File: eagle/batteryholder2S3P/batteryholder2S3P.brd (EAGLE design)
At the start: 144 x 90 mm, 12 parts, among them J3 POWER_JACKPTH_BREAD

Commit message: batteryholder boards minor changes
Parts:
- removed BT5, BT6, BT7: KEYSTONE_1048KEYSTONE_1048_0_0, Keystone - 1048:KEYSTONE_1048_0
- J3: value POWER_JACKPTH_BREAD -> 5.5x2.1mm Barrel; device SparkFun-Connectors:POWER_JACK_PTH_BREAD -> SparkFun-Connectors:POWER_JACK_SMD
- moved J3 6.00 mm to (141.5, 57.0), turned to 180 degrees
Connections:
- net BOTTOM_MINUS: now also BT1.2, BT1.4, BT2.2, J3.P$4; no longer BT5.1, BT5.3, BT6.1, BT6.3, BT7.1, BT7.3, J3.GND
- net TOP_MINUS: no longer BT5.2, BT5.4, BT6.2, BT6.4, BT7.2, BT7.4
- net TOP_PLUS: now also J3.VIN0; no longer BT1.2, BT1.4, BT2.2, J3.PWR
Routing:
- net TOP_PLUS: track 21.7 -> 18.2 mm
- net TOP_MINUS: vias 31 -> 0
- net BOTTOM_MINUS: vias 0 -> 66
- added copper zone on layer 1, net BOTTOM_MINUS
- removed copper zone on layer 16, net TOP_MINUS
- removed copper zone on layer 16, net TOP_PLUS
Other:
- board text added: "2S3P"
- board text added: "batteryholder 2S3P"
- board text added: "revision B"
- board text removed: "2S6P"

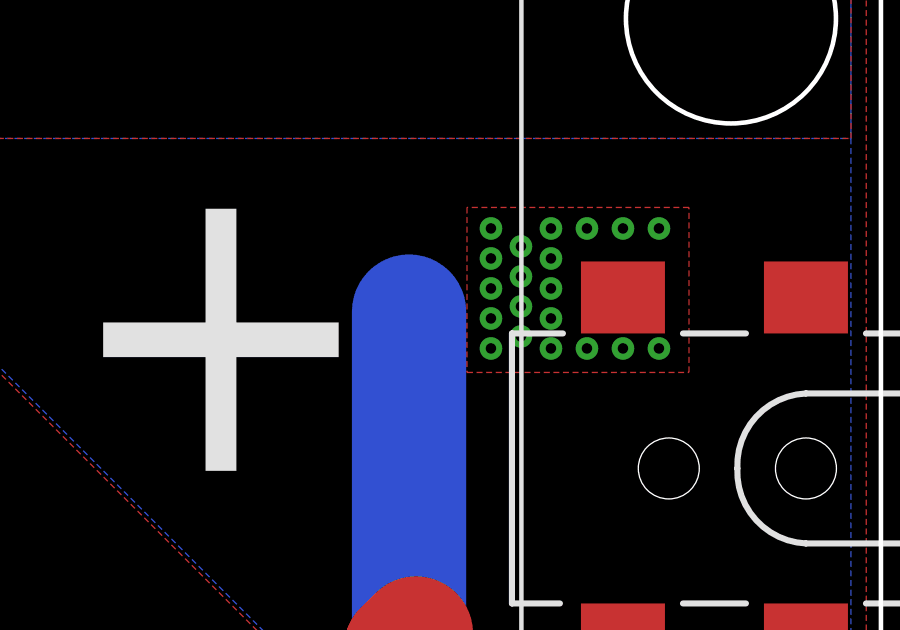
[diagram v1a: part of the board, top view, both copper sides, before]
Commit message: eagle: rename batteryholder vertical
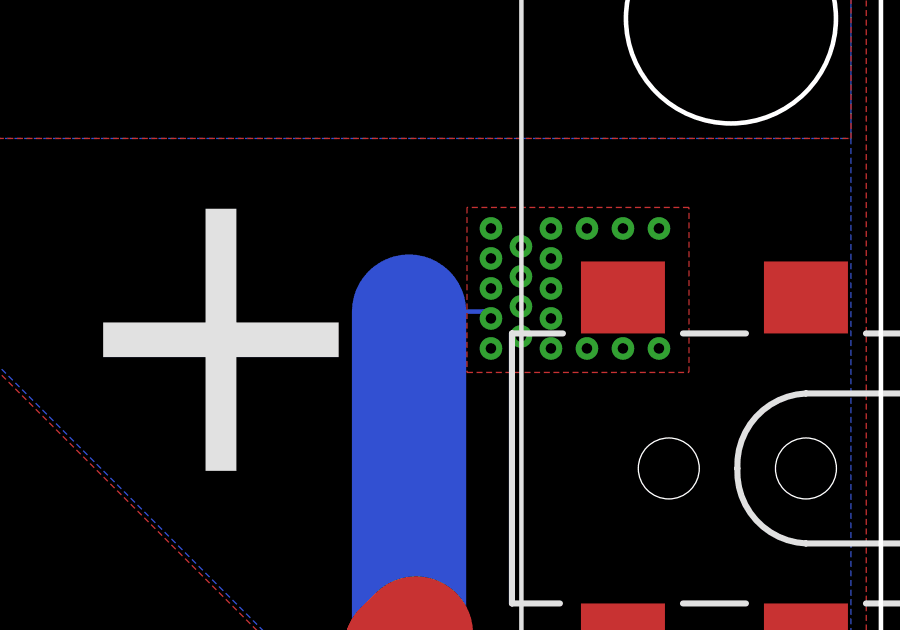
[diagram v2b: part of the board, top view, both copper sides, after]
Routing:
- net BOTTOM_MINUS: track 41.5 -> 44.4 mm
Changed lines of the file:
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@@
 <layer number="44" name="Drills" color="7" fill="1" visible="no" active="yes"/>
 <layer number="45" name="Holes" color="7" fill="1" visible="yes" active="yes"/>
-<layer number="46" name="Milling" color="3" fill="1" visible="no" active="yes"/>
+<layer number="46" name="Milling" color="3" fill="1" visible="yes" active="yes"/>
 <layer number="47" name="Measures" color="7" fill="1" visible="no" active="yes"/>
 <layer number="48" name="Document" color="7" fill="1" visible="no" active="yes"/>
@@
 <via x="135.4" y="61" extent="1-16" drill="0.35"/>
 <via x="136.6" y="61" extent="1-16" drill="0.35"/>
+<wire x1="128.27" y1="62.23" x2="130.77" y2="62.23" width="0.1524" layer="16"/>
+<wire x1="130.77" y1="62.23" x2="131" y2="62" width="0.1524" layer="16"/>
 </signal>
 </signals>
